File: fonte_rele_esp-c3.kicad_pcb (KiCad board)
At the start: 2 copper layers, 26 parts, among them J1 Screw_Terminal_01x03, J2 Conn_01x05_Pin, J3 Screw_Terminal_01x02, K1 G5LE-1, Q1 AO3400A, U1 AZ1117CH2-3.3, U2 HS-40012, U3 ESP32-C3-WROOM-02

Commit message: Atualizando fiduciais
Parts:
- added FID1: Fiducial, Fiducial:Fiducial_0.5mm_Mask1mm, F.Cu at (191.9, 150.4)
- added FID2: Fiducial, Fiducial:Fiducial_0.5mm_Mask1mm, F.Cu at (191.9, 153.0)
- added FID3: Fiducial, Fiducial:Fiducial_0.5mm_Mask1mm, F.Cu at (191.9, 155.5)
- added H1: MountingHole, MountingHole:MountingHole_2.2mm_M2, F.Cu at (196.0, 132.7)
- added H2: MountingHole, MountingHole:MountingHole_2.2mm_M2, F.Cu at (196.0, 138.7)
- added H3: MountingHole, MountingHole:MountingHole_2.2mm_M2, F.Cu at (196.0, 144.6)
- added H4: MountingHole, MountingHole:MountingHole_2.2mm_M2, F.Cu at (196.1, 152.1)
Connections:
- C1 pad 2: GNDPWR -> GND
- C2 pad 2: GNDPWR -> GND
- C3 pad 2: GNDPWR -> GND
- C4 pad 2: GNDPWR -> GND
- C5 pad 2: GNDPWR -> GND
- R4 pad 1: GNDPWR -> GND
- R5 pad 1: GNDPWR -> GND
- U1 pad 2: GNDPWR -> GND
- U2 pad 9: GNDPWR -> GND

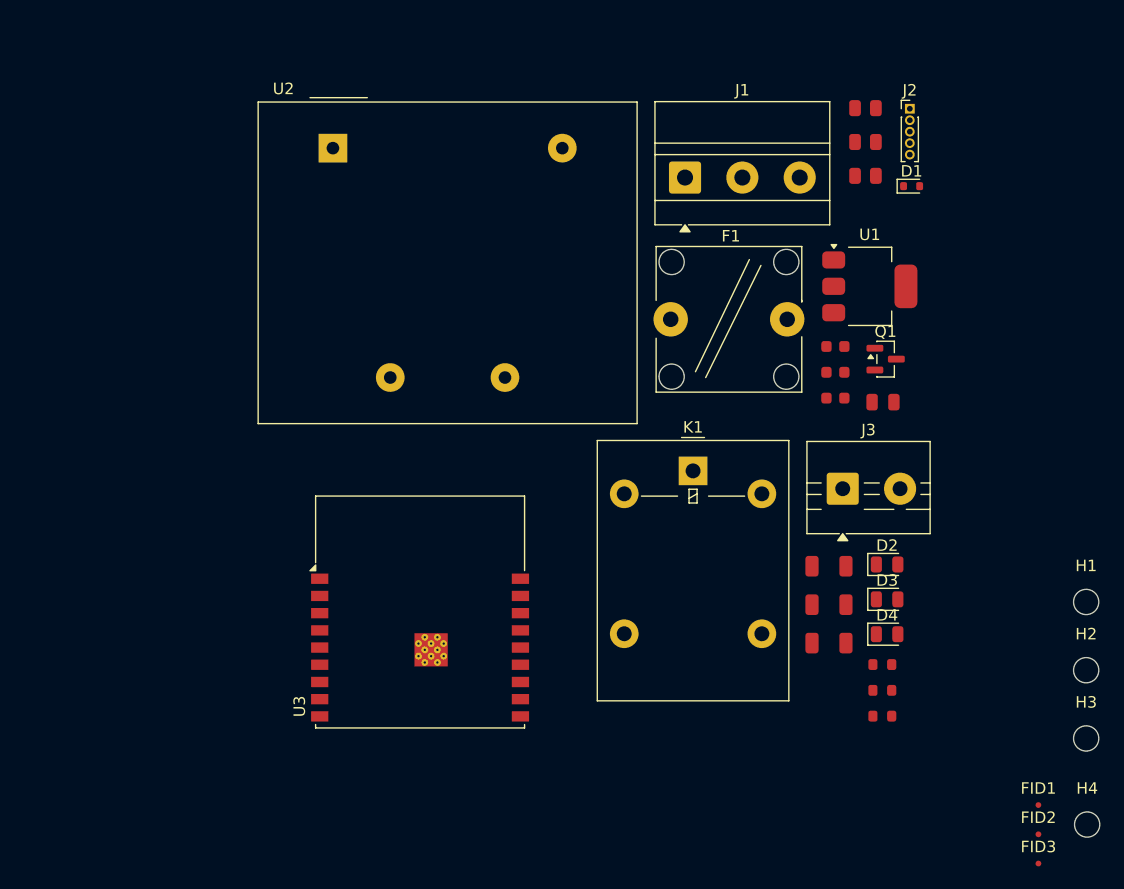
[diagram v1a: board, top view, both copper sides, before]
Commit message: Ajusta posição do símbolo de terra no esquemático
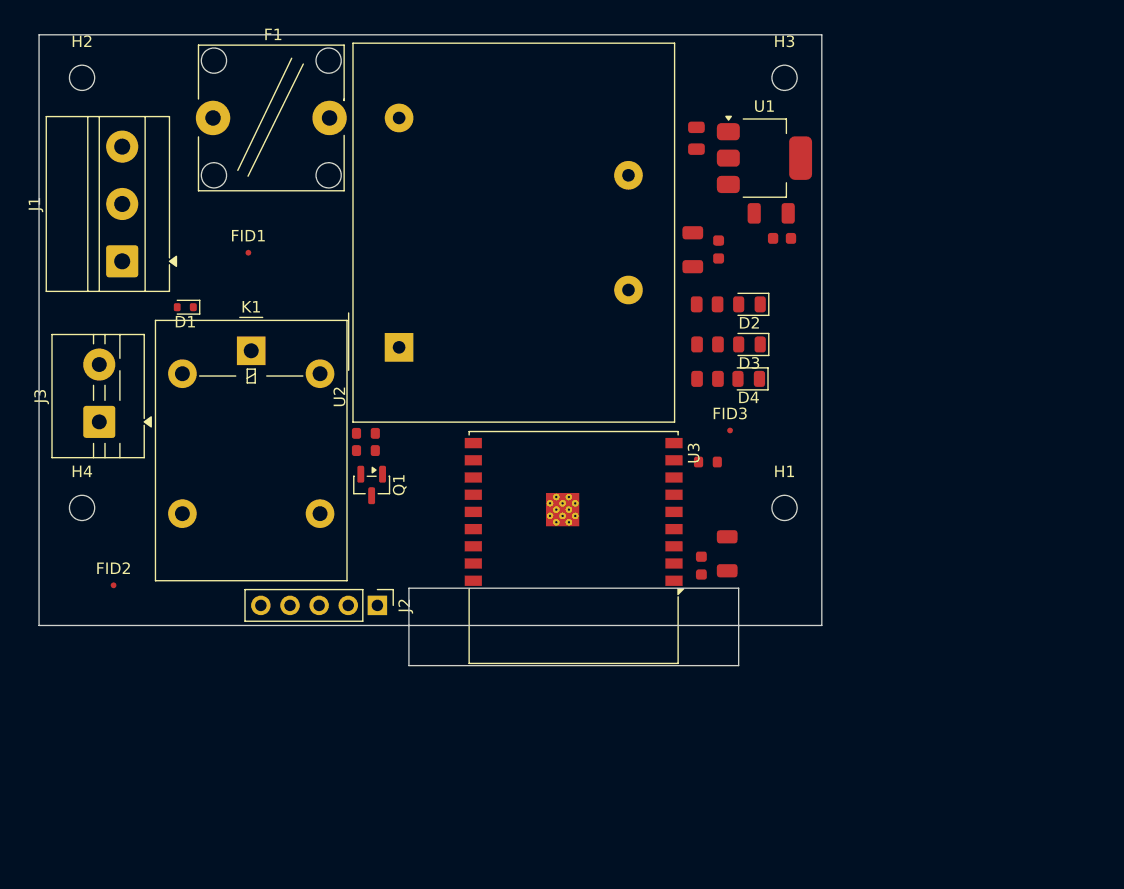
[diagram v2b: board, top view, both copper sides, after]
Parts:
- J2: footprint Connector_PinHeader_1.00mm:PinHeader_1x05_P1.00mm_Vertical -> Connector_PinHeader_2.54mm:PinHeader_1x05_P2.54mm_Vertical
- moved H2 101.6 mm to (108.5, 87.0)
- moved H4 91.9 mm to (108.5, 124.5)
- moved FID1 84.0 mm to (123.0, 102.2)
- moved FID2 83.5 mm to (111.2, 131.2)
- moved J3 65.1 mm to (110.0, 117.0), turned to 90 degrees
- moved D1 64.2 mm to (117.5, 107.0), turned to 180 degrees
- moved J2 63.5 mm to (134.2, 133.0), turned to -90 degrees
- moved H3 63.3 mm to (169.8, 87.0)
- moved R3 50.6 mm to (133.2, 119.5)
- moved R2 50.3 mm to (133.2, 118.0), turned to 180 degrees
- moved J1 49.6 mm to (112.0, 103.0), turned to 90 degrees
- moved FID3 46.4 mm to (165.0, 117.8)
- moved Q1 46.1 mm to (133.8, 122.5), turned to -90 degrees
- moved F1 43.6 mm to (119.9, 90.5)
- moved K1 39.9 mm to (123.2, 110.8)
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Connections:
- J1 pad 1: Earth -> N
- J1 pad 2: N -> Earth
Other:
- board outline added: 68.2 x 55 mm

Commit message: Move controle do relé de GPIO9 (strapping) pra GPIO0 e atualiza layout da PCB
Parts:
- moved C2 15.0 mm to (163.7, 87.0)
- moved C1 14.3 mm to (162.0, 87.7)
- moved C5 7.28 mm to (162.2, 101.2)
- moved C4 7.13 mm to (163.0, 103.2)
- moved C3 4.54 mm to (166.0, 90.0), turned to 180 degrees
- moved U1 4.20 mm to (164.2, 95.9), turned to -90 degrees
- moved D2 3.01 mm to (166.4, 109.8)
- moved D3 3.01 mm to (166.4, 107.2)
- moved R4 3.01 mm to (162.8, 109.8)
- moved R5 3.01 mm to (162.8, 107.2)
- moved FID1 2.93 mm to (124.0, 99.5)
- moved R1 1.35 mm to (164.4, 120.4)
- moved D4 1.03 mm to (166.4, 112.2)
- moved R6 1.03 mm to (162.8, 112.2)
- moved C6 0.75 mm to (164.8, 129.2)
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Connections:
- U3 pad 10: unconnected-(U3-IO10-Pad10) -> /RELE
- U3 pad 17: /RELE -> unconnected-(U3-IO1-Pad17)
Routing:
- net +12V: track 0.00 -> 47.3 mm
- net /BOOT: track 0.00 -> 41.1 mm, vias 0 -> 1
- net +3V3: track 0.00 -> 37.9 mm
- net N: track 0.00 -> 30.7 mm
- net /RX: track 0.00 -> 21.5 mm
- net /TX: track 0.00 -> 18.9 mm
- net /NA: track 0.00 -> 13.2 mm
- net Net-(J1-Pin_3): track 0.00 -> 8.96 mm
- net AC: track 0.00 -> 6.06 mm
- net Net-(D2-A): track 0.00 -> 1.84 mm
- net Net-(D3-A): track 0.00 -> 1.81 mm
- net Net-(D4-A): track 0.00 -> 1.74 mm

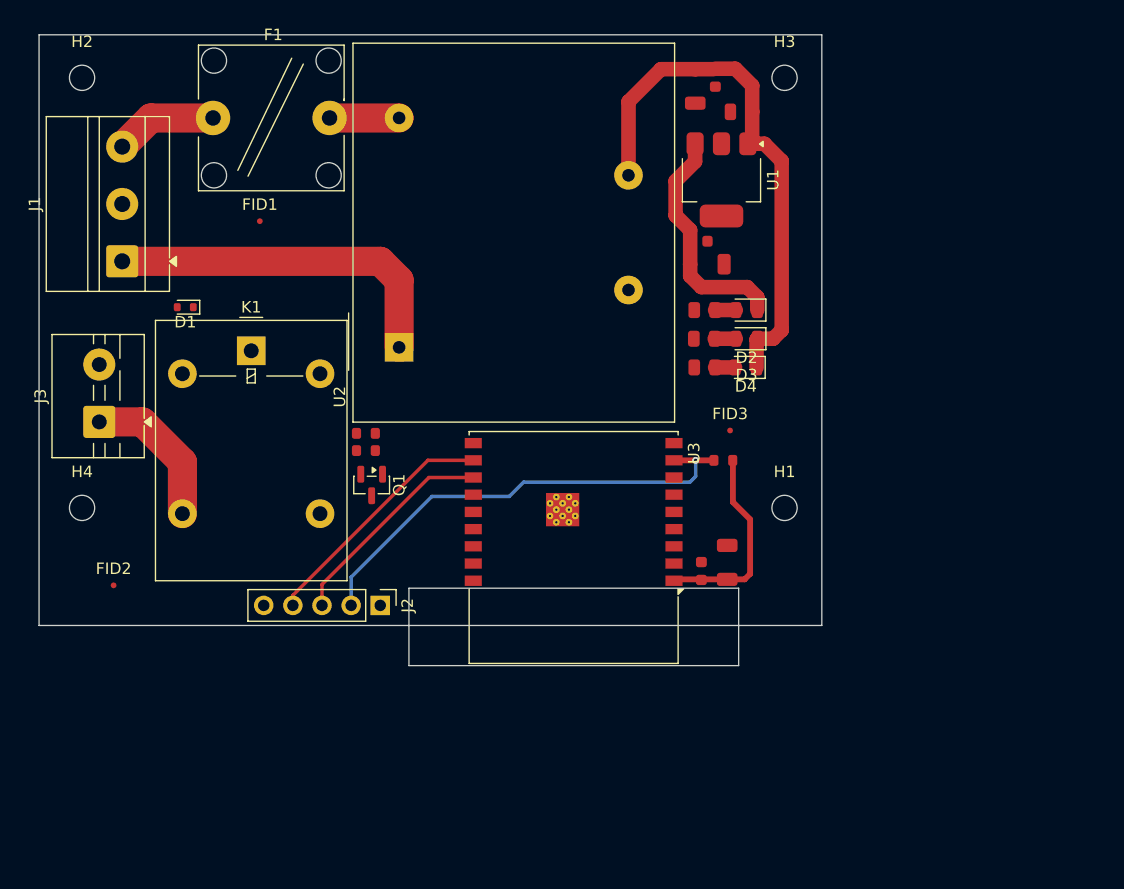
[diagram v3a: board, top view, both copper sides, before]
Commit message: Ajusta J3 (L_IN/L_OUT) e layout de PCB do driver do relé
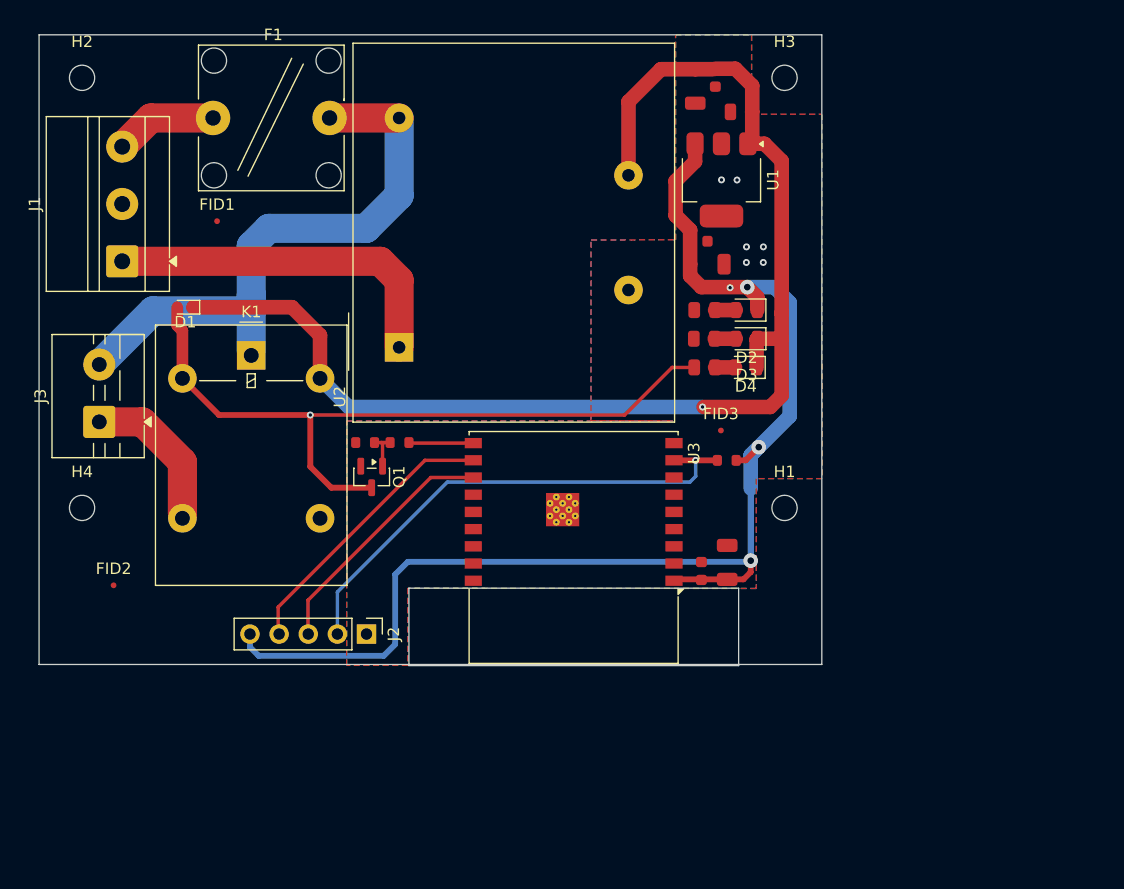
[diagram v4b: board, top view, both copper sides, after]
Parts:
- moved FID1 3.73 mm to (120.3, 99.5)
- moved R2 3.04 mm to (136.2, 118.8), turned to 0 degrees
- moved J2 2.77 mm to (133.3, 135.5)
- moved FID3 0.80 mm to (164.2, 117.8)
- moved R3 0.70 mm to (133.2, 118.8)
- moved Q1 0.70 mm to (133.8, 121.8)
- moved K1 0.41 mm to (123.2, 111.2)
- moved R1 0.30 mm to (164.7, 120.4)
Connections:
- D1 pad 2: Net-(D1-A) -> /DRAIN
- J3 pad 2: /L_OUT -> AC
- K1 pad 2: Net-(D1-A) -> /DRAIN
- Q1 pad 3: +12V -> /DRAIN
- R6 pad 1: +12V -> /DRAIN
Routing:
- net +3V3: track 37.9 -> 121.4 mm, vias 0 -> 4
- net /DRAIN: track 0.00 -> 64.3 mm, vias 0 -> 1
- net +12V: track 47.3 -> 109.7 mm, vias 0 -> 1
- net AC: track 6.06 -> 51.9 mm
- net /RELE: track 0.00 -> 5.68 mm
- net Net-(Q1-G): track 0.00 -> 3.46 mm
- net /RX: track 21.5 -> 24.7 mm
- net /TX: track 18.9 -> 21.8 mm
- net /BOOT: track 41.1 -> 44.0 mm
- net GND: vias 0 -> 6
- added copper zone on B.Cu, net GND
- added copper zone on F.Cu, net GND
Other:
- outline, holes or cut-outs redrawn

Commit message: Adiciona pull-up de 10k no EN do ESP32-C3 (R7)
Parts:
- added R7: 10kΩ, Resistor_SMD:R_0603_1608Metric, F.Cu at (162.4, 126.0)
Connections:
- U3 pad 2: unconnected-(U3-EN-Pad2) -> Net-(U3-EN)
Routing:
- net Net-(U3-EN): track 0.00 -> 3.83 mm
- net +3V3: track 121.4 -> 124.8 mm

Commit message: Continua layout da PCB
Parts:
- moved H1 10.6 mm to (169.6, 135.1)
- moved H4 10.6 mm to (108.4, 135.1)
- moved J1 0.61 mm to (112.6, 102.9)
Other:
- board size 68.2 x 55 mm -> 67.5 x 55 mm
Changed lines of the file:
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@@
 	(footprint "MountingHole:MountingHole_2.2mm_M2"
 		(layer "F.Cu")
-		(at 169.75 124.5)
+		(at 169.620232 135.077525)
 		(descr "Mounting Hole 2.2mm, M2, no annular, generated by kicad-footprint-generator mountinghole.py")
 		(tags "mountinghole M2")
@@
 	(footprint "MountingHole:MountingHole_2.2mm_M2"
 		(layer "F.Cu")
-		(at 108.5 124.5)
+		(at 108.370232 135.077525)
 		(descr "Mounting Hole 2.2mm, M2, no annular, generated by kicad-footprint-generator mountinghole.py")
 		(tags "mountinghole M2")
@@
 	(footprint "TerminalBlock_MetzConnect:TerminalBlock_MetzConnect_Type011_RT05503HBLC_1x03_P5.00mm_Horizontal"
 		(layer "F.Cu")
-		(at 112 103 90)
+		(at 112.6 102.9 90)
 		(descr "terminal block Metz Connect Type011_RT05503HBLC, 3 pins, pitch 5mm, size 15x10.5mm, drill diameter 1.4mm, pad diameter 2.8mm, https://americancableassemblies.com/content/metz/863188.PDF")
 		(tags "THT terminal block Metz Connect Type011_RT05503HBLC pitch 5mm size 15x10.5mm drill 1.4mm pad 2.8mm")
@@
 	)
 	(gr_rect
-		(start 104.75 83.25)
+		(start 105.5 83.25)
 		(end 173 138.1506)
 		(stroke
@@
 		(layer "F.Cu")
 		(pts
-			(xy 104.7496 132.1816) (xy 172.9994 132.1816)
+			(xy 105.5 83.25) (xy 105.5 138.15)
 		)
-		(height 14.8082)
+		(height -3.35)
+		(orientation 1)
+		(format
+			(prefix "")
+			(suffix "")
+			(units 3)
+			(units_format 0)
+			(precision 4)
+			(suppress_zeroes yes)
+		)
+		(style
+			(thickness 0.2)
+			(arrow_length 1.27)
+			(text_position_mode 0)
+			(arrow_direction outward)
+			(extension_height 0.58642)
+			(extension_offset 0.5)
+			(keep_text_aligned yes)
+		)
+		(gr_text "54,9"
+			(at 100.35 110.7 90)
+			(layer "F.Cu")
+			(effects
+				(font
+					(size 1.5 1.5)
+					(thickness 0.3)
+				)
+			)
+		)
+	)
+	(dimension
+		(type orthogonal)
+		(layer "F.Cu")
+		(pts
+			(xy 105.5 138.15) (xy 173 138.15)
+		)
+		(height 11.25)
 		(orientation 0)
 		(format
@@
 			(keep_text_aligned yes)
 		)
-		(gr_text "2687"
-			(at 138.8745 145.1898 0)
+		(gr_text "67,5"
+			(at 139.25 147.6 0)
 			(layer "F.Cu")
 			(effects
@@
 	)
 	(segment
+		(start 160.718 129.35)
+		(end 162.4 127.668)
+		(width 0.508)
+		(layer "F.Cu")
+		(net "Net-(U3-EN)")
+	)
+	(segment
+		(start 160.11 129.35)
+		(end 160.718 129.35)
+		(width 0.508)
+		(layer "F.Cu")
+		(net "Net-(U3-EN)")
+	)
+	(segment
+		(start 162.4 127.668)
+		(end 162.4 126.825)
+		(width 0.508)
+		(layer "F.Cu")
+		(net "Net-(U3-EN)")
+	)
+	(segment
 		(start 162 120.354956)
 		(end 160.114956 120.354956)
@@
 		(net "Net-(J1-Pin_3)")
 	)
-	(segment
-		(start 160.718 129.35)
-		(end 162.4 127.668)
-		(width 0.508)
-		(layer "F.Cu")
-		(net "Net-(U3-EN)")
-	)
-	(segment
-		(start 160.11 129.35)
-		(end 160.718 129.35)
-		(width 0.508)
-		(layer "F.Cu")
-		(net "Net-(U3-EN)")
-	)
-	(segment
-		(start 162.4 127.668)
-		(end 162.4 126.825)
-		(width 0.508)
-		(layer "F.Cu")
-		(net "Net-(U3-EN)")
-	)
 	(zone
 		(net "GND")
@@
 		(polygon
 			(pts
-				(xy 166.878 83.2612) (xy 166.878 90.17) (xy 172.9994 90.17) (xy 173.026124 121.9454) (xy 167.2844 121.9454)
+				(xy 166.878 83.2612) (xy 166.878 90.17) (xy 172.9994 90.17) (xy 173.03416 131.5) (xy 167.2844 131.5)
 				(xy 167.2844 131.522424) (xy 136.906 131.4958) (xy 136.906 138.2216) (xy 131.572 138.2216) (xy 131.572 116.9162)
 				(xy 160.02 116.9162) (xy 152.8826 116.8908) (xy 152.8826 101.1428) (xy 160.2486 101.1174) (xy 160.2486 83.2612)

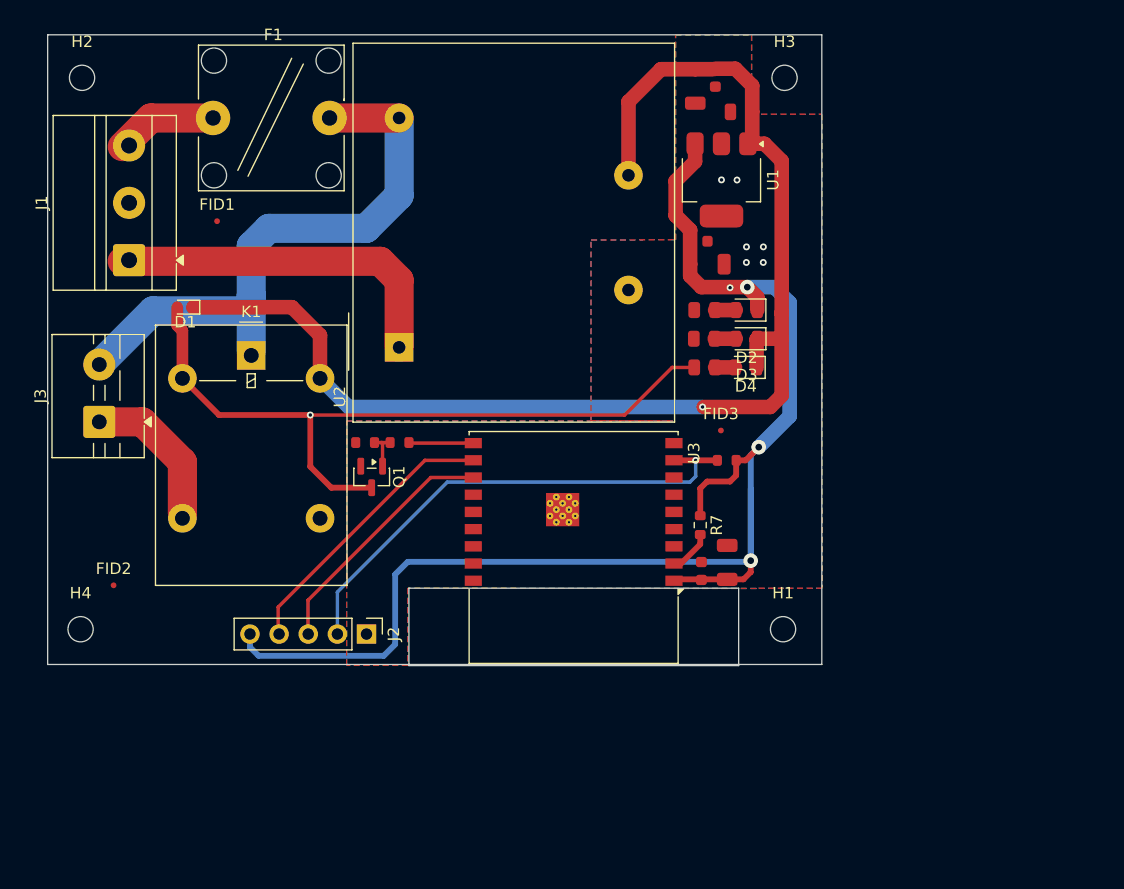
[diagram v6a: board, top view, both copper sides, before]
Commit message: Atualiza esquematico e PCB do fonte_rele_esp-c3
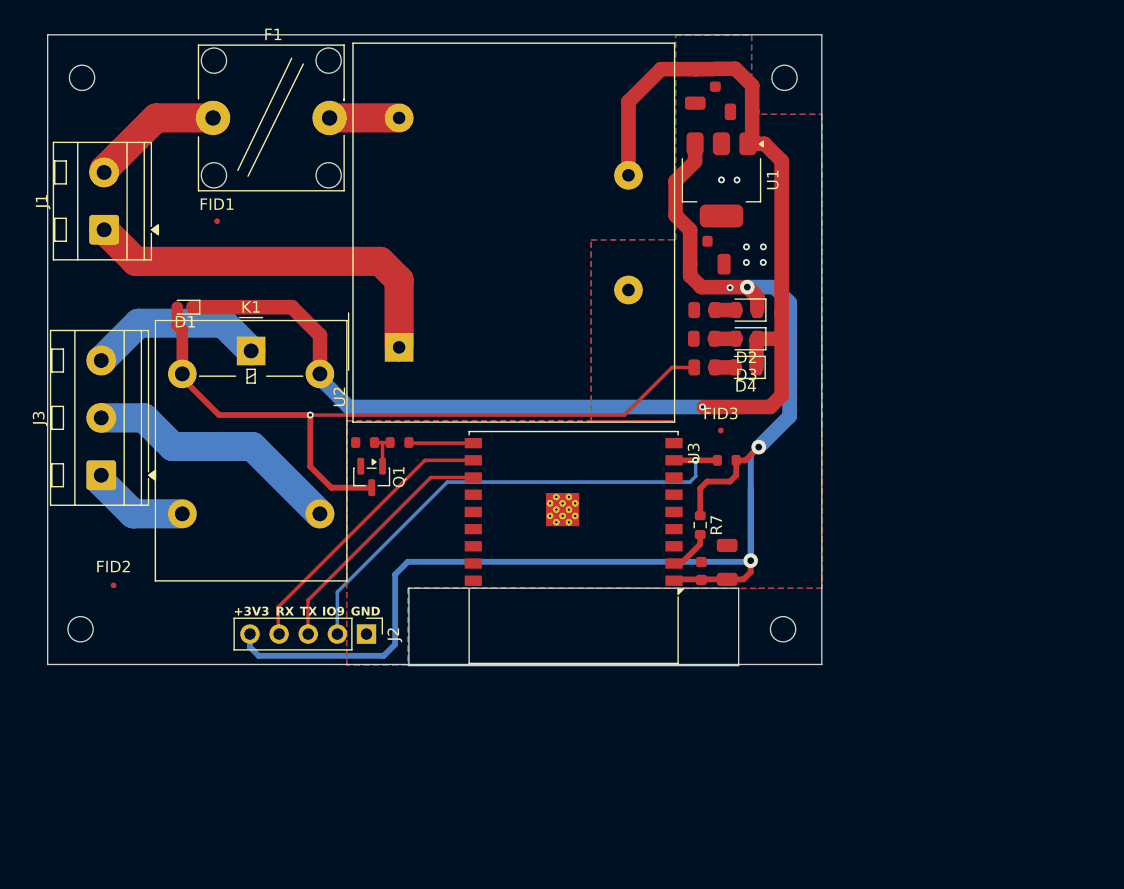
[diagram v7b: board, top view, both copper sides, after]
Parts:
- J1: value Screw_Terminal_01x03 -> Screw_Terminal_01x02; footprint TerminalBlock_MetzConnect:TerminalBlock_MetzConnect_Type011_RT05503HBLC_1x03_P5.00mm_Horizontal -> TerminalBlock_MetzConnect:TerminalBlock_MetzConnect_Type094_RT03502HBLU_1x02_P5.00mm_Horizontal
- J3: value Screw_Terminal_01x02 -> Screw_Terminal_01x03; footprint TerminalBlock:TerminalBlock_MaiXu_MX126-5.0-02P_1x02_P5.00mm -> TerminalBlock_MetzConnect:TerminalBlock_MetzConnect_Type094_RT03503HBLU_1x03_P5.00mm_Horizontal
- moved J3 4.65 mm to (110.2, 121.7)
- moved J1 3.43 mm to (110.4, 100.2)
- moved K1 0.39 mm to (123.2, 110.8)
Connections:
- F1 pad 1: Net-(J1-Pin_3) -> Net-(J1-Pin_2)
- J1 pad 2: Earth -> Net-(J1-Pin_2)
- J3 pad 2: AC -> /NF
- K1 pad 1: AC -> /COM
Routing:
- net AC: track 51.9 -> 6.06 mm
- net /NF: track 0.00 -> 22.5 mm
- net /COM: track 0.00 -> 15.4 mm
- net Net-(J1-Pin_2): track 0.00 -> 11.6 mm
- net Net-(J1-Pin_3): track 8.96 -> 0.00 mm
- net /NA: track 13.2 -> 8.80 mm
- net N: track 30.7 -> 33.4 mm
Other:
- board text added: "+3V3"
- board text added: "GND"
- board text added: "IO9"
- board text added: "RX"
- board text added: "TX"
